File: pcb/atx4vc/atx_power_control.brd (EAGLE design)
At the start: 86 x 70 mm, 59 parts, among them IC2 REG1117, IC3 STM32F042F4, IC4 MY_7905DT, J1 ATX24RH, SW1 324_SW, SW2 324_SW, SW3 324_SW, SW4 324_SW, SW5 324_SW, SW7 324_SW, U1 USBC_16P, U2 USBC_16P

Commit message: updated pcb headers
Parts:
- moved R13 14.4 mm to (73.4, 59.3), turned to 0 degrees
- moved JP2 1.27 mm to (52.6, 51.3)
- moved JP7 1.27 mm to (66.0, 51.3)
- moved R12 1.27 mm to (59.1, 57.0)
- moved U1 1.27 mm to (66.0, 58.7)
- moved F2 0.25 mm to (58.7, 44.3)
- moved F3 0.25 mm to (58.7, 27.6)
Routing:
- net N$34: track 12.2 -> 9.89 mm
- net N$35: track 47.0 -> 48.3 mm
- net N$15: track 63.8 -> 65.1 mm
- net N$16: track 44.3 -> 45.3 mm
- net N$7: track 17.8 -> 18.7 mm
- net N$6: track 27.7 -> 28.2 mm

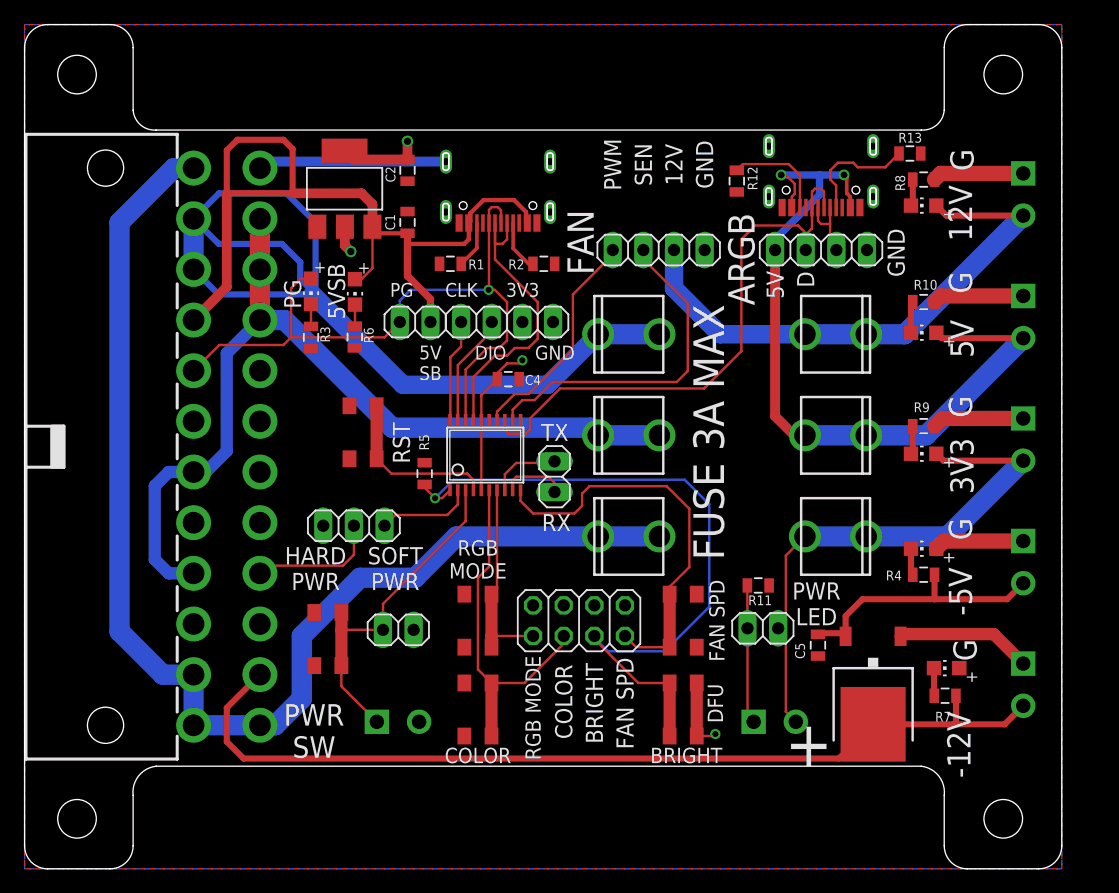
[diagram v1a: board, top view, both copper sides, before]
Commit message: added selector jumper for power-on detect
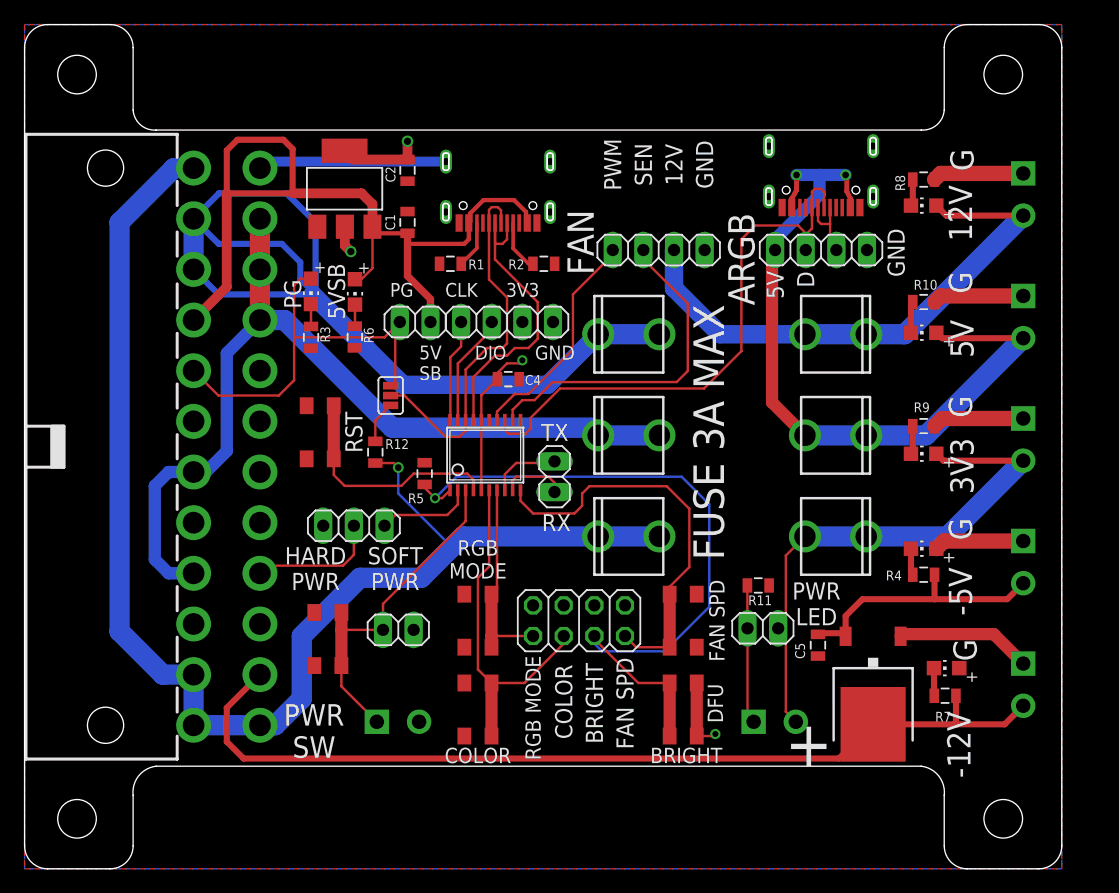
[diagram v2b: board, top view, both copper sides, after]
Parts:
- removed R13: 5.1K, joyAnalog:0805
- added JP4: JUMPER-32-3, SparkFun-Retired:SJ_3_PASTE2&3
- moved R12 37.5 mm to (29.1, 34.5), turned to 90 degrees
- moved SW3 3.56 mm to (24.5, 36.2)
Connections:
- removed net N$28: IC3.18, J1.8, JP3.1, LED3.A, U2.A6, U2.B6
- removed net N$32: R12.1, U1.B5
- removed net N$34: R13.1, U1.A5
- new net FFFF: J1.8, JP3.1, JP4.1, LED3.A
- new net N$30: JP4.3, R12.2
- new net USB_DP: IC3.18, JP4.2, U2.A6, U2.B6
- net GND: no longer R12.2, R13.2
- net N$14: now also R12.1
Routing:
- net N$28: track 57.0 -> 0.00 mm, vias 1 -> 0
- net FFFF: track 0.00 -> 34.1 mm
- net USB_DP: track 0.00 -> 31.2 mm
- net N$14: track 101.9 -> 112.4 mm, vias 0 -> 1
- net N$34: track 9.89 -> 0.00 mm
- net N$32: track 8.51 -> 0.00 mm
- net BUTTON1: track 14.0 -> 19.2 mm
- net N$30: track 0.00 -> 3.51 mm
- net N$15: track 65.1 -> 62.9 mm
- net BUTTON2: track 59.8 -> 60.3 mm

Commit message: adjusted power button and power LED
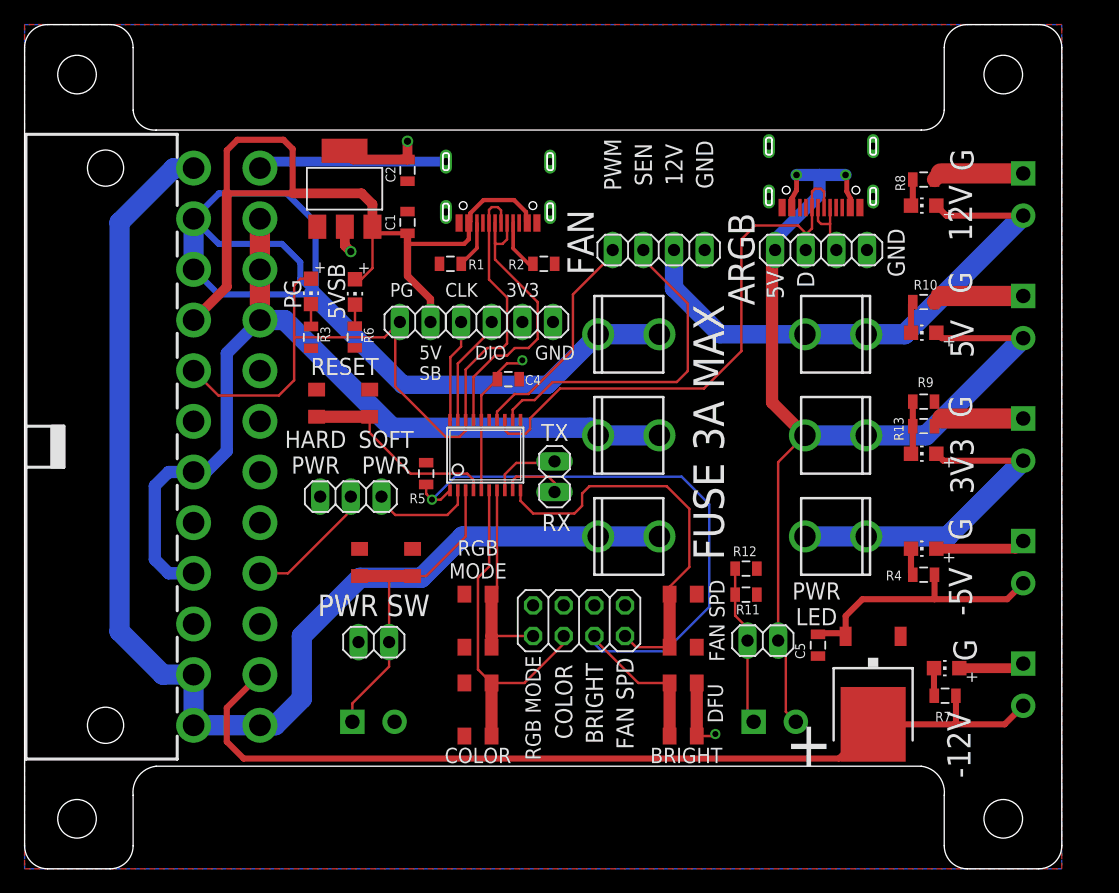
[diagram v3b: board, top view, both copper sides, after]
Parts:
- removed JP4: JUMPER-32-3, SparkFun-Retired:SJ_3_PASTE2&3
- added R13: 1K, SparkFun-Passives:0805
- R12: value 5.1K -> 1K; device joyAnalog:0805 -> SparkFun-Passives:0805
- moved R12 32.2 mm to (59.8, 24.9), turned to 180 degrees
- moved SW1 7.98 mm to (30.0, 25.4), turned to 180 degrees
- moved SW3 3.07 mm to (26.4, 38.6), turned to 180 degrees
- moved JP5 2.43 mm to (27.1, 30.9)
- moved JP6 2.27 mm to (29.0, 18.8), turned to 0 degrees
- moved J5 2.03 mm to (27.2, 12.2)
- moved R11 1.27 mm to (59.8, 22.7)
- moved JP1 1.02 mm to (61.2, 18.9)
- moved R5 0.13 mm to (33.3, 32.8)
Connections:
- removed net FFFF: J1.8, JP3.1, JP4.1, LED3.A
- removed net N$15: F1.3, F1.4, J7.2, JP7.1, LED7.A, U1.A4B9, U1.B4A9
- net GND: now also R12.1, R13.1
- net N$14: no longer R12.1
- net N$17: now also R12.2
- net N$18: now also R13.2
- net N$19: no longer J8.2, JP1.1
- net N$30: now also F1.3, F1.4, J7.2, J8.2, JP1.1, JP7.1, LED7.A, U1.A4B9, U1.B4A9; no longer JP4.3, R12.2
- net USB_DP: now also J1.8, JP3.1, LED3.A; no longer JP4.2
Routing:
- net N$30: track 3.51 -> 88.2 mm, vias 0 -> 2
- net N$15: track 62.9 -> 0.00 mm, vias 2 -> 0
- net FFFF: track 34.1 -> 0.00 mm
- net USB_DP: track 31.2 -> 65.1 mm
- net N$19: track 45.1 -> 28.1 mm
- net N$14: track 112.4 -> 101.9 mm, vias 1 -> 0
- net GND: track 57.1 -> 51.3 mm
- net BUTTON1: track 19.2 -> 16.8 mm
- net N$17: track 11.5 -> 13.8 mm
- net N$18: track 2.35 -> 4.38 mm
- net N$26: track 28.1 -> 27.3 mm
- net N$24: track 7.98 -> 8.72 mm
- net BUTTON2: track 60.3 -> 60.9 mm
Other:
- board text added: "RESET"
- board text removed: "RST"

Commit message: optimised traces routing for current carrying
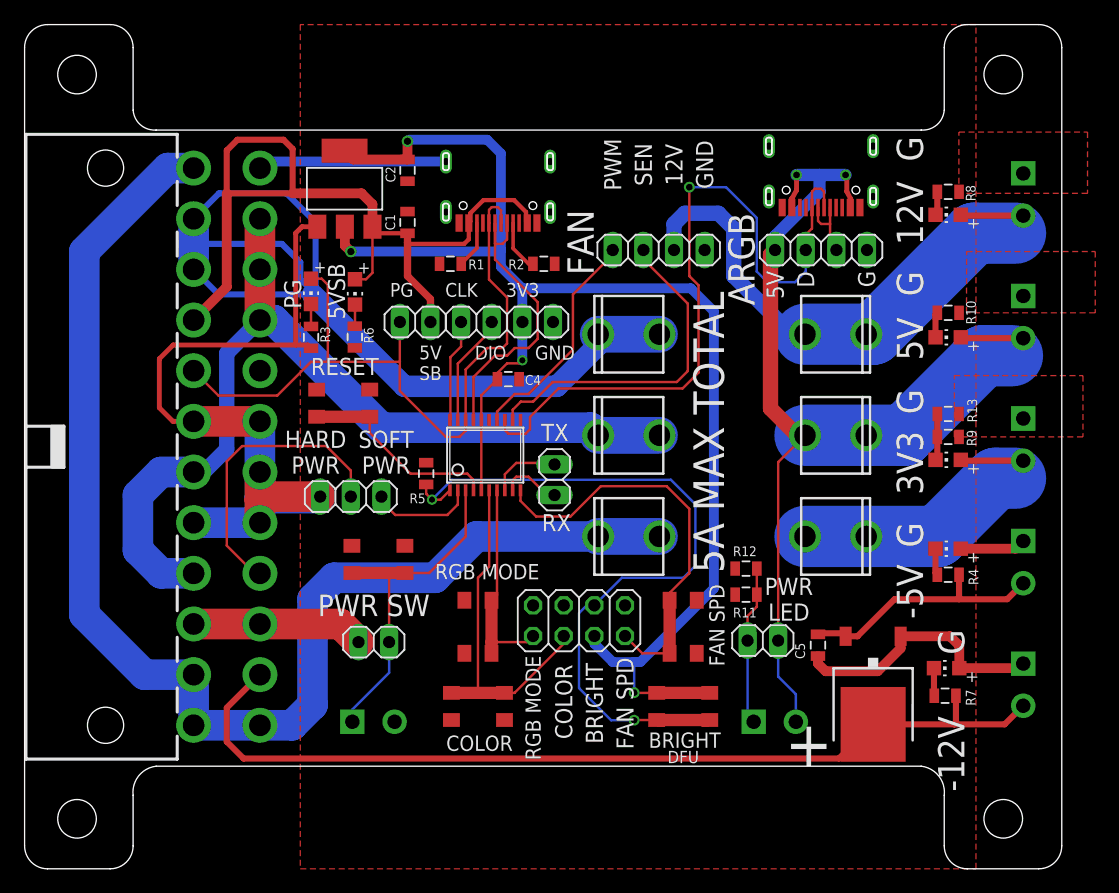
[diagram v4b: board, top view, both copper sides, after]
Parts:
- moved R13 2.27 mm to (76.6, 37.7)
- moved R8 2.27 mm to (76.6, 56.1)
- moved R10 2.22 mm to (76.6, 46.1)
- moved R9 2.22 mm to (76.6, 35.8)
- moved LED5 2.17 mm to (76.6, 54.2)
- moved LED6 2.09 mm to (76.6, 33.9)
- moved LED7 2.07 mm to (76.6, 44.1)
- moved LED1 2.03 mm to (76.6, 26.5)
- moved R4 2.03 mm to (76.6, 24.4)
- moved SW1 0.68 mm to (29.3, 25.7)
- moved SW5 0.51 mm to (37.6, 20.1)
- moved SW7 0.51 mm to (54.6, 20.1)
- moved SW2 0.25 mm to (37.6, 13.5), turned to 180 degrees
- moved SW4 0.25 mm to (54.6, 13.5), turned to 180 degrees
- moved JP10 0.25 mm to (43.9, 32.3)
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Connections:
- net USB_DP renamed PG
- net +3V3: now also JP9.4; no longer JP9.3
- net BUTTON2: now also JP9.3; no longer JP9.4
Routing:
- net +3V3: track 28.1 -> 122.9 mm
- net GND: track 51.3 -> 123.0 mm
- net N$25: track 10.8 -> 24.5 mm
- net N$35: track 48.3 -> 60.6 mm, vias 0 -> 1
- net N$14: track 101.9 -> 107.6 mm
- net N$16: track 45.3 -> 47.7 mm
- net N$10: track 74.4 -> 76.3 mm
- net N$19: track 28.1 -> 26.4 mm
- net PG: track 65.1 -> 63.4 mm
- net N$30: track 88.2 -> 86.8 mm
- net N$11: track 22.0 -> 21.0 mm
- net N$26: track 27.3 -> 28.1 mm
- net N$22: track 16.6 -> 17.4 mm
- net N$17: track 13.8 -> 13.2 mm
- net N$20: track 2.60 -> 2.09 mm
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- removed copper zone on layer 16, net +3V3
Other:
- board text added: "5A MAX TOTAL"
- board text removed: "FUSE 3A MAX"

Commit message: minor cleanup
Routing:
- net GND: track 123.0 -> 122.0 mm
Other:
- board text added: "ATX4VC.com dekuNukem SEPT 2022 PT4"
- board text removed: "ATX4VC.COM dekuNukem SEPT 2022 PT4"
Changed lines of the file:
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@@
 <text x="33.655" y="41.9562" size="1.143" layer="25" rot="R180" align="center">5V
 SB</text>
-<text x="6.096" y="35.052" size="2.54" layer="26" rot="MR90" align="center">ATX4VC.COM
+<text x="6.096" y="35.052" size="2.54" layer="26" rot="MR90" align="center">ATX4VC.com
 dekuNukem SEPT 2022
 PT4</text>
@@
 <text x="22.2296" y="47.6542" size="1.4224" layer="25" rot="R90" align="center">PG</text>
 <text x="46.101" y="51.943" size="2.1844" layer="25" rot="R90" align="center">FAN</text>
-<text x="59.436" y="50.546" size="2.1844" layer="25" rot="R90" align="center">ARGB</text>
+<text x="59.563" y="53.213" size="2.1844" layer="25" rot="R90" align="center">ARGB</text>
 <text x="38.354" y="24.638" size="1.27" layer="25" align="center">RGB MODE</text>
 <text x="37.719" y="10.414" size="1.27" layer="25" align="center">COLOR</text>
@@
 <wire x1="22.479" y1="52.715" x2="22.479" y2="43.434" width="0.4064" layer="1"/>
 <polygon width="0.2032" layer="1" thermals="no">
-<vertex x="78.105" y="51.181"/>
-<vertex x="88.773" y="51.181"/>
+<vertex x="78.105" y="51.943"/>
+<vertex x="88.773" y="51.943"/>
 <vertex x="88.773" y="46.101"/>
 <vertex x="78.105" y="46.101"/>
 </polygon>
 <polygon width="0.2032" layer="1" thermals="no">
-<vertex x="77.47" y="61.087"/>
-<vertex x="88.138" y="61.087"/>
-<vertex x="88.138" y="56.007"/>
-<vertex x="77.47" y="56.007"/>
+<vertex x="77.47" y="61.849"/>
+<vertex x="88.138" y="61.849"/>
+<vertex x="88.138" y="56.261"/>
+<vertex x="77.47" y="56.261"/>
 </polygon>
 <polygon width="0.2032" layer="1" thermals="no">
-<vertex x="77.089" y="40.894"/>
-<vertex x="87.757" y="40.894"/>
-<vertex x="87.757" y="35.814"/>
-<vertex x="77.089" y="35.814"/>
-</polygon>
-<wire x1="65.786" y1="17.642" x2="65.786" y2="17.018" width="0.8128" layer="1"/>
-<wire x1="65.786" y1="17.018" x2="66.421" y2="16.383" width="0.8128" layer="1"/>
-<wire x1="66.421" y1="16.383" x2="70.739" y2="16.383" width="0.8128" layer="1"/>
-<wire x1="72.638" y1="18.282" x2="72.638" y2="19.278" width="0.8128" layer="1"/>
-<wire x1="70.739" y1="16.383" x2="72.638" y2="18.282" width="0.8128" layer="1"/>
+<vertex x="77.089" y="41.783"/>
+<vertex x="87.757" y="41.783"/>
+<vertex x="87.757" y="35.941"/>
+<vertex x="77.089" y="35.941"/>
+</polygon>
+<wire x1="66.675" y1="17.272" x2="66.305" y2="17.642" width="0.8128" layer="1"/>
+<wire x1="65.786" y1="17.642" x2="66.305" y2="17.642" width="0.8128" layer="1"/>
+<wire x1="66.675" y1="17.272" x2="71.882" y2="17.272" width="0.8128" layer="1"/>
+<wire x1="72.638" y1="18.028" x2="72.638" y2="19.278" width="0.8128" layer="1"/>
+<wire x1="71.882" y1="17.272" x2="72.638" y2="18.028" width="0.8128" layer="1"/>
 <wire x1="72.638" y1="19.278" x2="76.734" y2="19.278" width="0.8128" layer="1"/>
 <wire x1="77.504" y1="18.508" x2="77.504" y2="16.637" width="0.8128" layer="1"/>
 <wire x1="76.734" y1="19.278" x2="77.504" y2="18.508" width="0.8128" layer="1"/>
 <wire x1="14.014" y1="28.7" x2="19.514" y2="28.7" width="2.54" layer="16"/>
-<wire x1="19.514" y1="32.9" x2="19.514" y2="30.734" width="2.54" layer="16"/>
-<wire x1="19.514" y1="30.734" x2="19.514" y2="28.7" width="2.54" layer="16"/>
+<wire x1="19.514" y1="32.9" x2="19.514" y2="30.861" width="2.54" layer="16"/>
+<wire x1="19.514" y1="30.861" x2="19.514" y2="28.7" width="2.54" layer="16"/>
 <wire x1="19.514" y1="37.1" x2="19.514" y2="32.9" width="2.54" layer="16"/>
-<wire x1="19.514" y1="30.734" x2="24.384" y2="30.734" width="2.54" layer="16"/>
-<wire x1="24.384" y1="30.734" x2="24.511" y2="30.861" width="2.54" layer="16"/>
 <wire x1="19.514" y1="32.9" x2="19.514" y2="30.607" width="2.54" layer="1"/>
 <wire x1="19.514" y1="30.607" x2="19.514" y2="28.7" width="2.54" layer="1"/>
 <wire x1="19.514" y1="30.607" x2="19.768" y2="30.861" width="2.54" layer="1"/>
 <wire x1="19.768" y1="30.861" x2="24.511" y2="30.861" width="2.54" layer="1"/>
+<wire x1="24.511" y1="30.861" x2="19.514" y2="30.861" width="1.524" layer="16"/>
 </signal>
 <signal name="+3V3">
@@
 <contactref element="R4" pad="1"/>
 <contactref element="J4" pad="2"/>
-<wire x1="72.136" y1="22.352" x2="69.062" y2="19.278" width="0.508" layer="1"/>
-<wire x1="68.078" y1="19.278" x2="69.062" y2="19.278" width="0.508" layer="1"/>
 <wire x1="82.804" y1="23.678" x2="81.478" y2="22.352" width="0.508" layer="1"/>
 <wire x1="81.478" y1="22.352" x2="77.481" y2="22.352" width="0.508" layer="1"/>
-<wire x1="77.481" y1="22.352" x2="72.136" y2="22.352" width="0.508" layer="1"/>
 <wire x1="77.481" y1="24.384" x2="77.481" y2="22.352" width="0.508" layer="1"/>
 <wire x1="68.078" y1="19.278" x2="67.824" y2="19.532" width="0.508" layer="1"/>
 <wire x1="67.824" y1="19.532" x2="65.876" y2="19.532" width="0.508" layer="1"/>
 <wire x1="65.876" y1="19.532" x2="65.786" y2="19.442" width="0.508" layer="1"/>
+<wire x1="77.481" y1="22.352" x2="77.47" y2="22.352" width="0.508" layer="1"/>
+<wire x1="77.47" y1="22.352" x2="76.327" y2="21.209" width="0.508" layer="1"/>
+<wire x1="76.327" y1="21.209" x2="71.755" y2="21.209" width="0.508" layer="1"/>
+<wire x1="71.755" y1="21.209" x2="69.824" y2="19.278" width="0.508" layer="1"/>
+<wire x1="69.824" y1="19.278" x2="68.078" y2="19.278" width="0.508" layer="1"/>
 </signal>
 <signal name="N$8">

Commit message: minor cleanup
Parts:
- moved SW3 0.92 mm to (27.2, 38.1)
- moved C4 0.25 mm to (39.9, 40.6)
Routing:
- net +3V3: track 122.9 -> 151.5 mm, vias 4 -> 5
- net GND: track 122.0 -> 145.5 mm
- net N$25: track 24.5 -> 10.6 mm
- net N$27: track 34.2 -> 25.5 mm
- net BUTTON2: track 61.2 -> 59.0 mm
- net BUTTON1: track 16.8 -> 16.0 mm
- net PG: track 63.4 -> 64.1 mm
